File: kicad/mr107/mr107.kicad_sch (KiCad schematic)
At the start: 70 parts, among them J1 USB_A, J10 L-KLS12, J2 gnd, J3 mosi, J4 miso, J5 sclk, J6 reset, J7 gnd, J8 gnd, J9 PW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

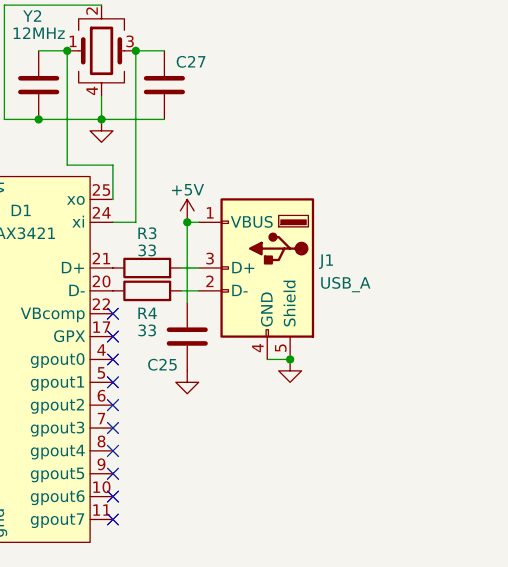
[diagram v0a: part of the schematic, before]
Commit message: изменено:      AVR/mr107_/mr107_.ino 	новый файл:    kicad/mr107/bom/ibom.html 	изменено:      kicad/mr107/gerber/Border.gbr 	изменено:      kicad/mr107/gerber/Bottom.gbr 	изменено:      kicad/mr107/gerber/MaskBottom.gbr 	изменено:      kicad/mr107/gerber/MaskTop.gbr 	изменено:      kicad/mr107/gerber/NCData.drl 	изменено:      kicad/mr107/gerber/Top.gbr 	изменено:      kicad/mr107/gerber/mk-gerber.sh 	изменено:      kicad/mr107/gerber/mk-gerber.sh~ 	изменено:      kicad/mr107/gerber/mr107-job.gbrjob 	изменено:      kicad/mr107/gerber/mr107.zip 	удалено:       kicad/mr107/mr107-backups/mr107-2023-12-05_182551.zip 	удалено:       kicad/mr107/mr107-backups/mr107-2023-12-05_183551.zip 	удалено:       kicad/mr107/mr107-backups/mr107-2023-12-05_184551.zip 	удалено:       kicad/mr107/mr107-backups/mr107-2023-12-05_190040.zip 	удалено:       kicad/mr107/mr107-backups/mr107-2023-12-06_163733.zip 	удалено:       kicad/mr107/mr107-backups/mr107-2023-12-06_164916.zip 	удалено:       kicad/mr107/mr107-backups/mr107-2023-12-06_165817.zip 	удалено:       kicad/mr107/mr107-backups/mr107-2023-12-06_185613.zip 	удалено:       kicad/mr107/mr107-backups/mr107-2023-12-06_190115.zip 	удалено:       kicad/mr107/mr107-backups/mr107-2023-12-07_163716.zip 	удалено:       kicad/mr107/mr107-backups/mr107-2023-12-07_164901.zip 	удалено:       kicad/mr107/mr107-backups/mr107-2023-12-10_204652.zip 	удалено:       kicad/mr107/mr107-backups/mr107-2023-12-12_102834.zip 	изменено:      kicad/mr107/mr107.kicad_pcb 	изменено:      kicad/mr107/mr107.kicad_prl 	изменено:      kicad/mr107/mr107.kicad_sch
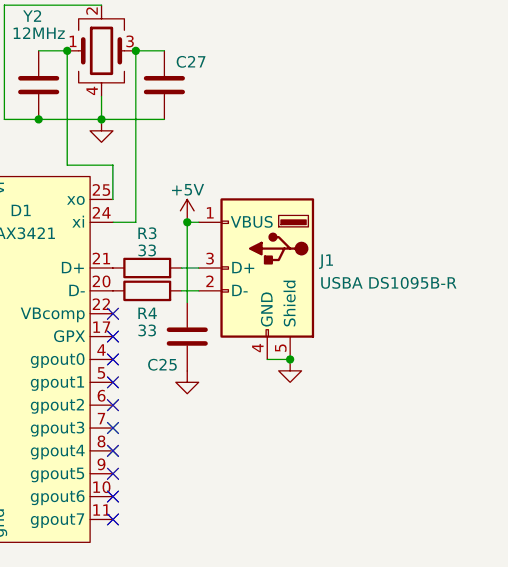
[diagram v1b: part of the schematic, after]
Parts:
- C29: value 10n -> 1n 2kV
- J1: value USB_A -> USBA DS1095B-R
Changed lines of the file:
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@@
       (effects (font (size 1.27 1.27)) (justify right))
     )
-    (property "Value" "USB_A" (id 1) (at 156.972 74.0922 0)
+    (property "Value" "USBA DS1095B-R" (id 1) (at 156.972 74.0922 0)
       (effects (font (size 1.27 1.27)) (justify right))
     )
@@
       (effects (font (size 1.27 1.27)) (justify left))
     )
-    (property "Value" "10n" (id 1) (at 131.826 168.7072 0)
+    (property "Value" "1n 2kV" (id 1) (at 131.826 168.7072 0)
       (effects (font (size 1.27 1.27)) (justify left) hide)
     )
@@
     )
     (path "/763d8361-8986-45bf-b18b-0b17b4962c9b"
-      (reference "C29") (unit 1) (value "10n") (footprint "Capacitor_SMD:C_0805_2012Metric")
+      (reference "C29") (unit 1) (value "1n 2kV") (footprint "Capacitor_SMD:C_0805_2012Metric")
     )
     (path "/67255374-0f11-491c-9146-82123903f89b"
@@
     )
     (path "/440b4971-7b5b-47ed-ad44-551052a4160f"
-      (reference "J1") (unit 1) (value "USB_A") (footprint "Connector_USB:USB_A_CONNFLY_DS1095-WNR0")
+      (reference "J1") (unit 1) (value "USBA DS1095B-R") (footprint "Connector_USB:USB_A_CONNFLY_DS1095-WNR0")
     )
     (path "/e9da7ccc-3797-430a-9dc0-42cc3a5fb4ee"

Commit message: изменено:      kicad/mr107/bom/ibom.html 	удалено:       kicad/mr107/gerber/Border.gbr 	удалено:       kicad/mr107/gerber/Bottom.gbr 	удалено:       kicad/mr107/gerber/MaskBottom.gbr 	удалено:       kicad/mr107/gerber/MaskTop.gbr 	удалено:       kicad/mr107/gerber/NCData.drl 	удалено:       kicad/mr107/gerber/Top.gbr 	изменено:      kicad/mr107/gerber/mk-gerber.sh 	удалено:       kicad/mr107/gerber/mk-gerber.sh~ 	удалено:       kicad/mr107/gerber/mr107-job.gbrjob 	изменено:      kicad/mr107/gerber/mr107.zip 	удалено:       kicad/mr107/mr107-backups/mr107-2023-12-07_165931.zip 	удалено:       kicad/mr107/mr107-backups/mr107-2023-12-07_170641.zip 	изменено:      kicad/mr107/mr107.kicad_pcb 	изменено:      kicad/mr107/mr107.kicad_prl 	изменено:      kicad/mr107/mr107.kicad_sch 	удалено:       kicad/mr107_802.3af/mr107-backups/mr107-2023-12-09_164959.zip
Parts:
- C29: footprint Capacitor_SMD:C_0805_2012Metric -> Capacitor_SMD:C_1206_3216Metric
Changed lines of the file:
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@@
       (effects (font (size 1.27 1.27)) (justify left) hide)
     )
-    (property "Footprint" "Capacitor_SMD:C_0805_2012Metric" (id 2) (at 129.8702 170.815 0)
+    (property "Footprint" "Capacitor_SMD:C_1206_3216Metric" (id 2) (at 129.8702 170.815 0)
       (effects (font (size 1.27 1.27)) hide)
     )
@@
     )
     (path "/763d8361-8986-45bf-b18b-0b17b4962c9b"
-      (reference "C29") (unit 1) (value "1n 2kV") (footprint "Capacitor_SMD:C_0805_2012Metric")
+      (reference "C29") (unit 1) (value "1n 2kV") (footprint "Capacitor_SMD:C_1206_3216Metric")
     )
     (path "/67255374-0f11-491c-9146-82123903f89b"

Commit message: изменено:      AVR/mr107_/mr107_.ino 	удалено:       kicad/mr107/mr107-backups/mr107-2023-12-09_164959.zip 	удалено:       kicad/mr107/mr107-backups/mr107-2023-12-09_165959.zip 	удалено:       kicad/mr107/mr107-backups/mr107-2023-12-09_205345.zip 	удалено:       kicad/mr107/mr107-backups/mr107-2023-12-10_205653.zip 	удалено:       kicad/mr107/mr107-backups/mr107-2023-12-10_210653.zip 	удалено:       kicad/mr107/mr107-backups/mr107-2023-12-10_211653.zip 	удалено:       kicad/mr107/mr107-backups/mr107-2023-12-10_212653.zip 	удалено:       kicad/mr107/mr107-backups/mr107-2023-12-10_213653.zip 	удалено:       kicad/mr107/mr107-backups/mr107-2023-12-11_153542.zip 	удалено:       kicad/mr107/mr107-backups/mr107-2023-12-11_155328.zip 	удалено:       kicad/mr107/mr107-backups/mr107-2023-12-11_160439.zip 	удалено:       kicad/mr107/mr107-backups/mr107-2023-12-11_172044.zip 	изменено:      kicad/mr107/mr107.kicad_sch
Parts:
- J2: value gnd -> RxD
- J8: value gnd -> TxD
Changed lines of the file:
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@@
       (effects (font (size 1.27 1.27)) (justify left) hide)
     )
-    (property "Value" "gnd" (id 1) (at 67.945 82.55 0)
+    (property "Value" "TxD" (id 1) (at 67.945 82.55 0)
       (effects (font (size 1.27 1.27)) (justify left) hide)
     )
@@
       (effects (font (size 1.27 1.27)) (justify left) hide)
     )
-    (property "Value" "gnd" (id 1) (at 67.945 80.01 0)
+    (property "Value" "RxD" (id 1) (at 67.945 80.01 0)
       (effects (font (size 1.27 1.27)) (justify left) hide)
     )
@@
     )
     (path "/e9da7ccc-3797-430a-9dc0-42cc3a5fb4ee"
-      (reference "J2") (unit 1) (value "gnd") (footprint "lib:conn_mini")
+      (reference "J2") (unit 1) (value "RxD") (footprint "lib:conn_mini")
     )
     (path "/b1b279b2-1c2b-42de-b5c3-1ee4e48562f8"
@@
     )
     (path "/10cdcf9b-9a0c-40bc-b22a-126eaa868ca7"
-      (reference "J8") (unit 1) (value "gnd") (footprint "lib:conn_mini")
+      (reference "J8") (unit 1) (value "TxD") (footprint "lib:conn_mini")
     )
     (path "/e018ac67-8fcb-4fb8-82e0-2d9626cab1ff"

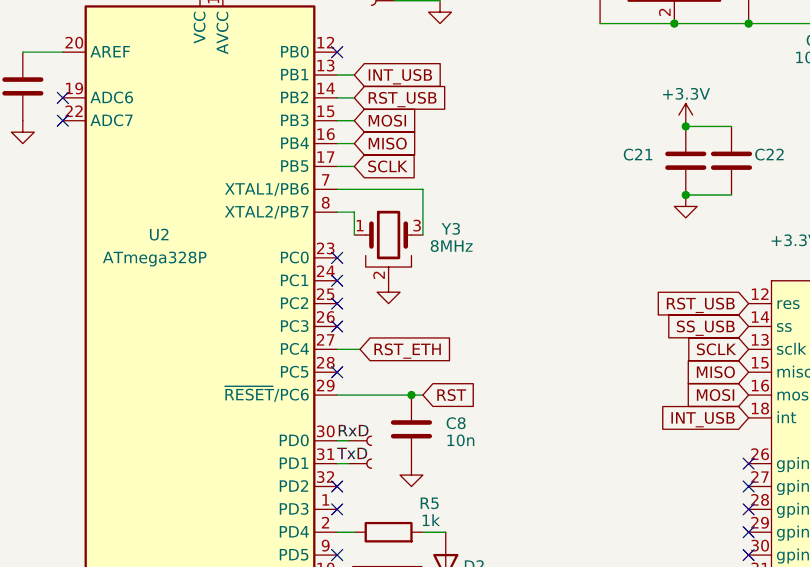
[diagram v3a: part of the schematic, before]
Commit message: изменено:      AVR/mr107_EEPROMCFG/mr107_EEPROMCFG.ino 	изменено:      kicad/mr107/mr107.kicad_sch
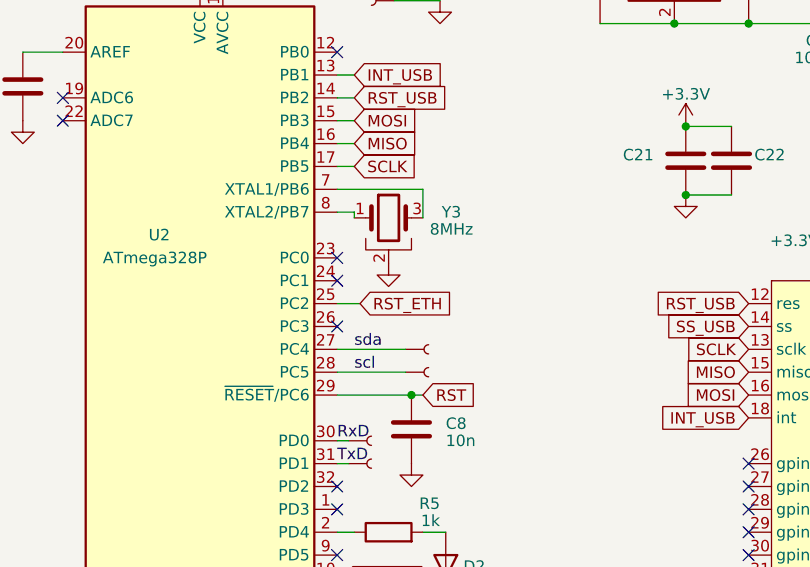
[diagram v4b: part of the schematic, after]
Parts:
- added J? (x2): mosi, lib:conn_mini, symbol My-Library:Conn
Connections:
- net RST_ETH: now also U2.25 (PC2); no longer U2.27 (PC4)
- net scl: now reaches U2.28 (PC5)
- net scl: now also J?.1
- new net sda: J?.1, U2.27 (PC4)
- no-connect marks 39 -> 37
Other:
- moved on the sheet: Y3
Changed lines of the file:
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@@
   (no_connect (at 133.985 92.71))
   (no_connect (at 133.985 90.17))
-  (no_connect (at 62.865 72.39))
   (no_connect (at 50.165 145.415))
   (no_connect (at 50.165 178.435))
@@
   (no_connect (at 50.165 180.975))
   (no_connect (at 108.585 100.33))
-  (no_connect (at 62.865 64.77))
   (no_connect (at 62.865 87.63))
   (no_connect (at 108.585 97.79))
@@
     (stroke (width 0) (type default) (color 0 0 0 0))
   )
-  (wire (pts (xy 72.39 52.07) (xy 72.39 57.15))
+  (wire (pts (xy 72.39 52.07) (xy 72.39 55.245))
     (stroke (width 0) (type default) (color 0 0 0 0))
   )
@@
     (stroke (width 0) (type default) (color 0 0 0 0))
   )
-  (wire (pts (xy 62.865 69.85) (xy 65.405 69.85))
-    (stroke (width 0) (type default) (color 0 0 0 0))
-  )
   (wire (pts (xy 151.13 82.55) (xy 153.67 82.55))
     (stroke (width 0) (type default) (color 0 0 0 0))
@@
     (stroke (width 0) (type default) (color 0 0 0 0))
   )
-  (wire (pts (xy 64.77 54.61) (xy 64.77 57.15))
+  (wire (pts (xy 64.77 54.61) (xy 64.77 55.245))
     (stroke (width 0) (type default) (color 0 0 0 0))
   )
@@
     (stroke (width 0) (type default) (color 0 0 0 0))
   )
+  (wire (pts (xy 62.865 72.39) (xy 70.485 72.39))
+    (stroke (width 0) (type default) (color 0 0 0 0))
+  )
   (wire (pts (xy 46.99 142.875) (xy 50.165 142.875))
     (stroke (width 0) (type default) (color 0 0 0 0))
   )
+  (wire (pts (xy 62.865 64.77) (xy 65.405 64.77))
+    (stroke (width 0) (type default) (color 0 0 0 0))
+  )
   (wire (pts (xy 100.965 117.475) (xy 104.14 117.475))
     (stroke (width 0) (type default) (color 0 0 0 0))
@@
   )
   (wire (pts (xy 86.995 183.515) (xy 86.995 186.055))
+    (stroke (width 0) (type default) (color 0 0 0 0))
+  )
+  (wire (pts (xy 62.865 69.85) (xy 70.485 69.85))
     (stroke (width 0) (type default) (color 0 0 0 0))
   )
@@
     (effects (font (size 1.27 1.27)) (justify left bottom))
   )
+  (label "sda" (at 64.77 69.85 0)
+    (effects (font (size 1.27 1.27)) (justify left bottom))
+  )
   (label "RxD" (at 62.865 80.01 0)
+    (effects (font (size 1.27 1.27)) (justify left bottom))
+  )
+  (label "scl" (at 64.77 72.39 0)
     (effects (font (size 1.27 1.27)) (justify left bottom))
   )
@@
     )
   )
-  (global_label "RST_ETH" (shape input) (at 65.405 69.85 0) (fields_autoplaced)
+  (global_label "RST_ETH" (shape input) (at 65.405 64.77 0) (fields_autoplaced)
     (effects (font (size 1.27 1.27)) (justify left))
-    (property "Обозначения листов" "${INTERSHEET_REFS}" (id 0) (at 75.68 69.7706 0)
+    (property "Обозначения листов" "${INTERSHEET_REFS}" (id 0) (at 75.68 64.6906 0)
       (effects (font (size 1.27 1.27)) (justify left) hide)
     )
@@
     (pin "2")
   )
-  (symbol (lib_id "power:GND") (at 68.58 62.23 0) (unit 1)
-    (in_bom yes) (on_board yes) (fields_autoplaced)
-    (property "Reference" "#PWR0115" (id 0) (at 68.58 68.58 0)
-      (effects (font (size 1.27 1.27)) hide)
-    )
-    (property "Value" "GND" (id 1) (at 68.58 66.6734 0)
-      (effects (font (size 1.27 1.27)) hide)
-    )
-    (property "Footprint" "" (id 2) (at 68.58 62.23 0)
-      (effects (font (size 1.27 1.27)) hide)
-    )
-    (property "Datasheet" "" (id 3) (at 68.58 62.23 0)
+  (symbol (lib_id "power:GND") (at 68.58 60.325 0) (unit 1)
+    (in_bom yes) (on_board yes) (fields_autoplaced)
+    (property "Reference" "#PWR0115" (id 0) (at 68.58 66.675 0)
+      (effects (font (size 1.27 1.27)) hide)
+    )
+    (property "Value" "GND" (id 1) (at 68.58 64.7684 0)
+      (effects (font (size 1.27 1.27)) hide)
+    )
+    (property "Footprint" "" (id 2) (at 68.58 60.325 0)
+      (effects (font (size 1.27 1.27)) hide)
+    )
+    (property "Datasheet" "" (id 3) (at 68.58 60.325 0)
       (effects (font (size 1.27 1.27)) hide)
     )
@@
     (pin "2")
   )
-  (symbol (lib_id "Device:Crystal_GND2") (at 68.58 57.15 0) (unit 1)
-    (in_bom yes) (on_board yes)
-    (property "Reference" "Y3" (id 0) (at 75.565 56.515 0))
-    (property "Value" "8MHz" (id 1) (at 75.565 58.42 0))
-    (property "Footprint" "Crystal:Resonator_SMD_Murata_CSTxExxV-3Pin_3.0x1.1mm" (id 2) (at 68.58 57.15 0)
-      (effects (font (size 1.27 1.27)) hide)
-    )
-    (property "Datasheet" "~" (id 3) (at 68.58 57.15 0)
+  (symbol (lib_id "Device:Crystal_GND2") (at 68.58 55.245 0) (unit 1)
+    (in_bom yes) (on_board yes)
+    (property "Reference" "Y3" (id 0) (at 75.565 54.61 0))
+    (property "Value" "8MHz" (id 1) (at 75.565 56.515 0))
+    (property "Footprint" "Crystal:Resonator_SMD_Murata_CSTxExxV-3Pin_3.0x1.1mm" (id 2) (at 68.58 55.245 0)
+      (effects (font (size 1.27 1.27)) hide)
+    )
+    (property "Datasheet" "~" (id 3) (at 68.58 55.245 0)
       (effects (font (size 1.27 1.27)) hide)
     )
@@
     (pin "1")
     (pin "2")
+  )
+  (symbol (lib_id "My-Library:Conn") (at 73.025 69.85 0) (unit 1)
+    (in_bom yes) (on_board yes)
+    (property "Reference" "J?" (id 0) (at 73.7362 69.0153 0)
+      (effects (font (size 1.27 1.27)) (justify left) hide)
+    )
+    (property "Value" "mosi" (id 1) (at 74.295 69.85 0)
+      (effects (font (size 1.27 1.27)) (justify left) hide)
+    )
+    (property "Footprint" "lib:conn_mini" (id 2) (at 74.295 73.66 0)
+      (effects (font (size 1.27 1.27)) hide)
+    )
+    (property "Datasheet" "~" (id 3) (at 73.025 69.85 0)
+      (effects (font (size 1.27 1.27)) hide)
+    )
+    (pin "1")
   )
   (symbol (lib_id "My-Library:Conn") (at 66.675 23.495 180) (unit 1)
@@
     (pin "2")
   )
+  (symbol (lib_id "My-Library:Conn") (at 73.025 72.39 0) (unit 1)
+    (in_bom yes) (on_board yes)
+    (property "Reference" "J?" (id 0) (at 73.7362 71.5553 0)
+      (effects (font (size 1.27 1.27)) (justify left) hide)
+    )
+    (property "Value" "mosi" (id 1) (at 74.295 72.39 0)
+      (effects (font (size 1.27 1.27)) (justify left) hide)
+    )
+    (property "Footprint" "lib:conn_mini" (id 2) (at 74.295 76.2 0)
+      (effects (font (size 1.27 1.27)) hide)
+    )
+    (property "Datasheet" "~" (id 3) (at 73.025 72.39 0)
+      (effects (font (size 1.27 1.27)) hide)
+    )
+    (pin "1")
+  )
   (symbol (lib_id "Device:C") (at 106.68 48.895 0) (unit 1)
     (in_bom yes) (on_board yes)
@@
       (reference "J10") (unit 1) (value "L-KLS12") (footprint "MyLibrary:KLS12-108")
     )
+    (path "/62840a42-d90d-427c-ad9f-a984bc00595d"
+      (reference "J?") (unit 1) (value "mosi") (footprint "lib:conn_mini")
+    )
+    (path "/b7efb4eb-5304-4752-b042-629f4172654c"
+      (reference "J?") (unit 1) (value "mosi") (footprint "lib:conn_mini")
+    )
     (path "/2be56d09-aac9-4f41-8d95-54c125ebb9b4"
